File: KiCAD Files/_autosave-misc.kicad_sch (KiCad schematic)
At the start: 16 parts, among them U1 K230_Rewired, U6 GT-USB-7013A03, Y1 32.768KHz, Y2 32.768KHz

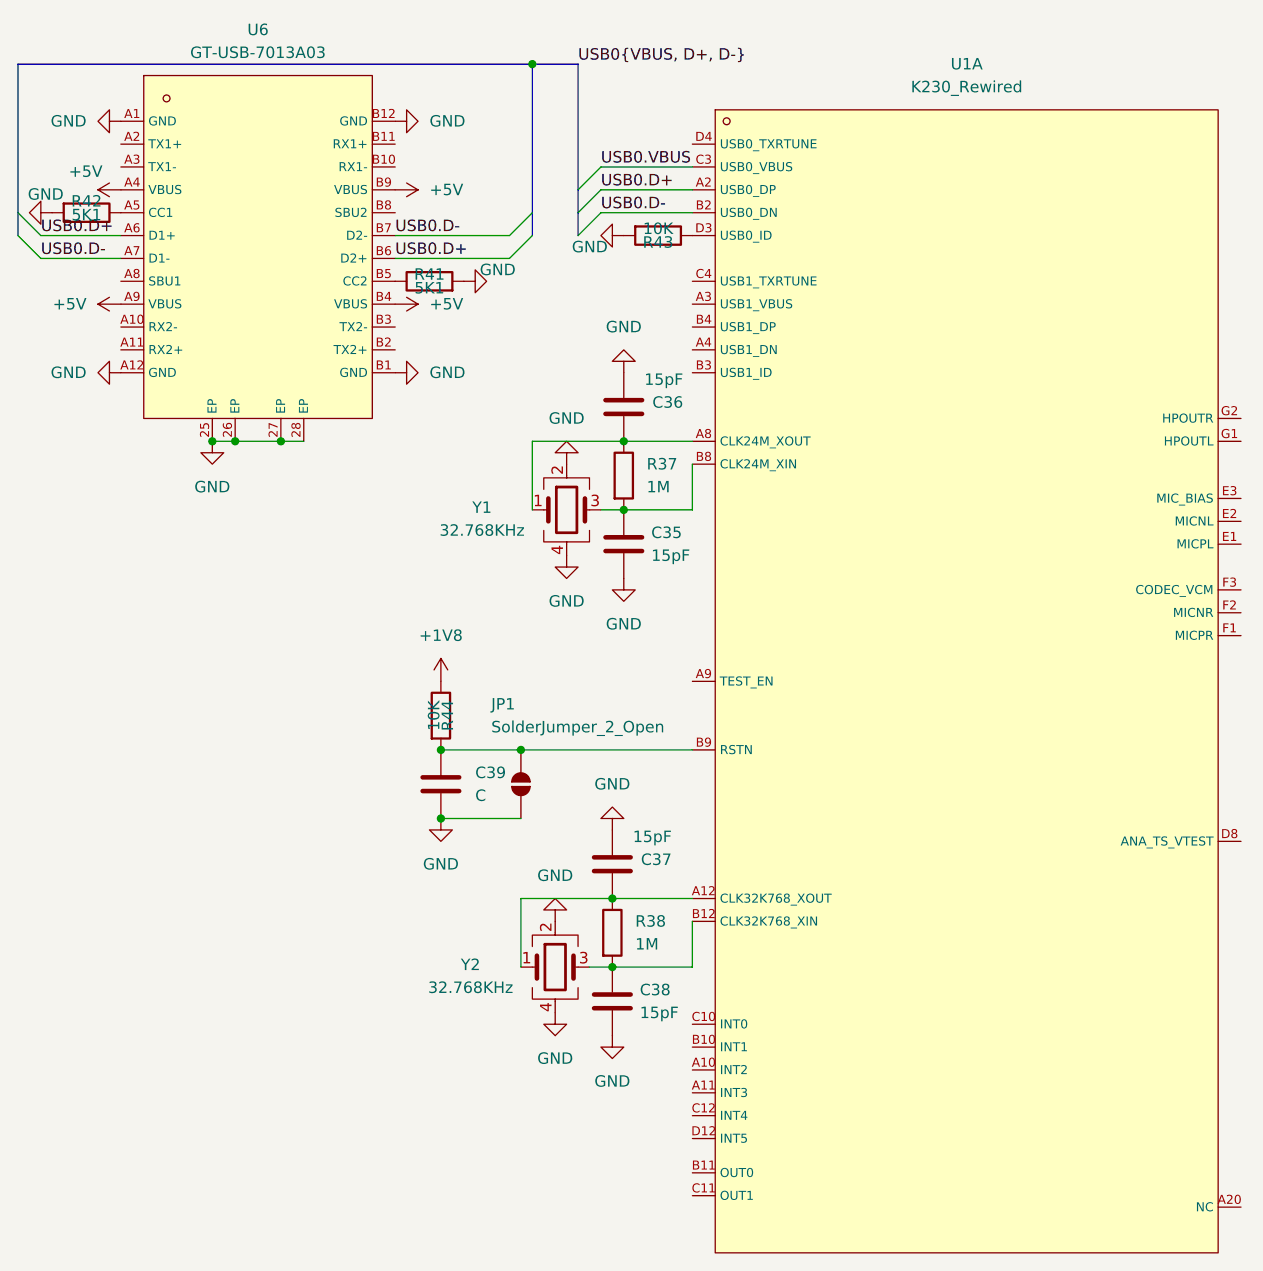
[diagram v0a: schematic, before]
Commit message: more peripherals
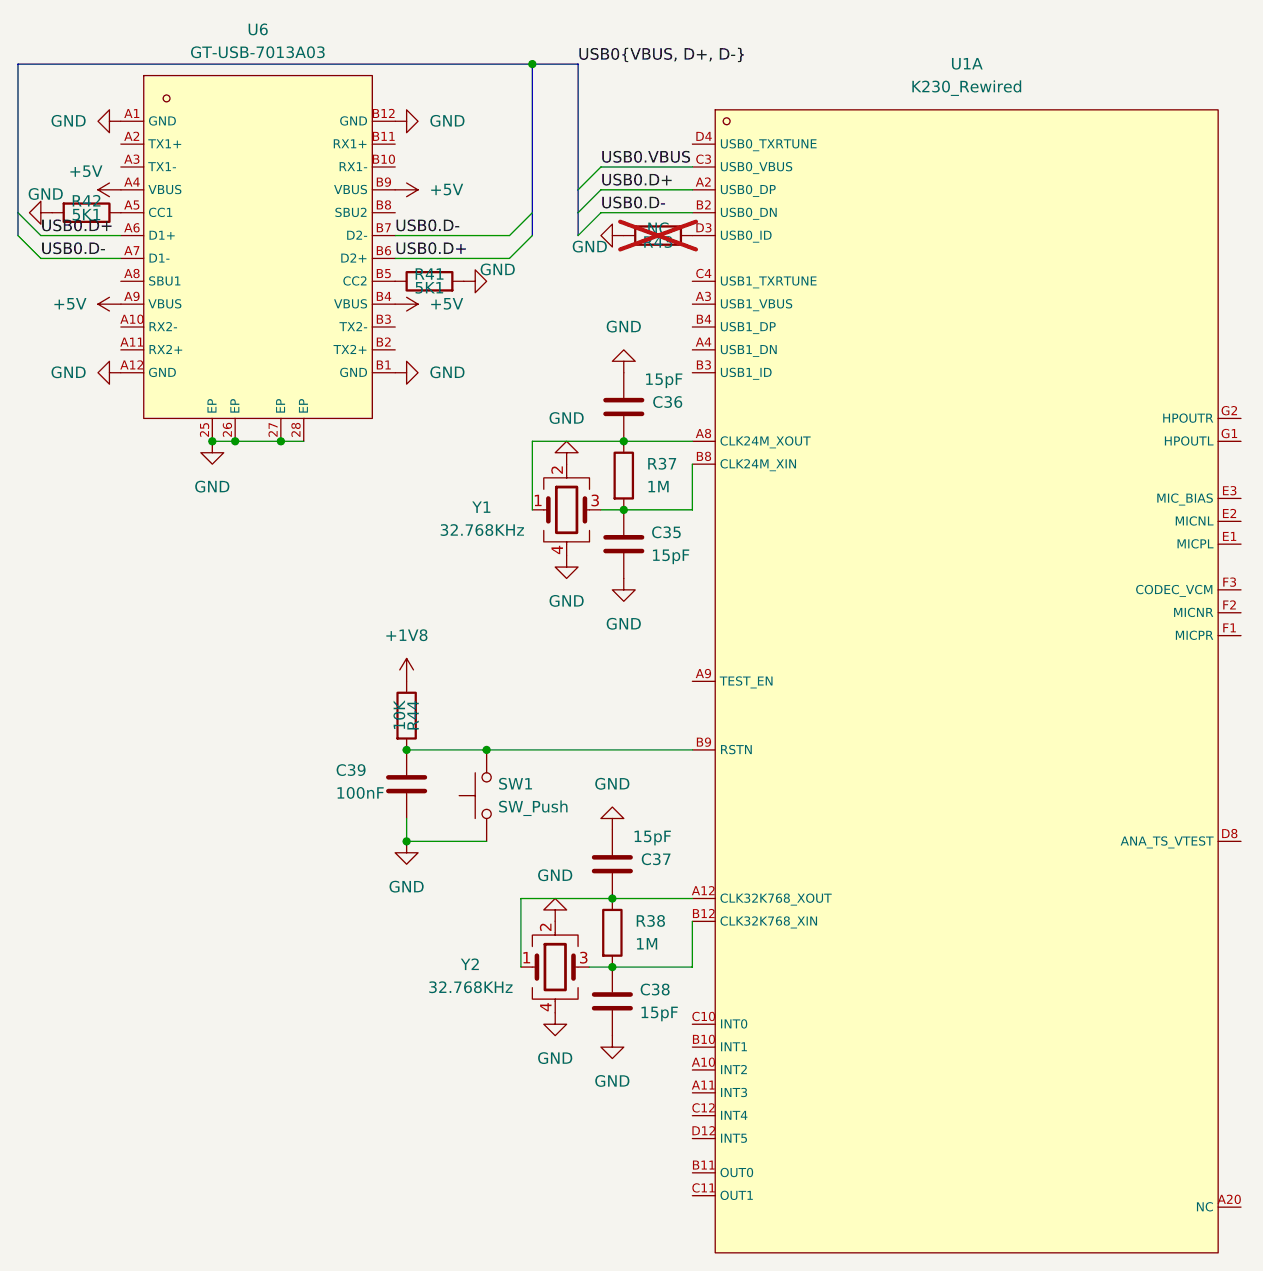
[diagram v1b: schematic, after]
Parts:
- removed JP1: SolderJumper_2_Open, Jumper:SolderJumper-2_P1.3mm_Open_TrianglePad1.0x1.5mm, symbol Jumper:SolderJumper_2_Open
- added SW1: SW_Push, Button_Switch_THT:SW_PUSH_1P1T_6x3.5mm_H4.3_APEM_MJTP1243, symbol Switch:SW_Push
- C39: value C -> 100nF
- R43: value 10K -> NC; now not fitted; now left out of the parts list
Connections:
- net GND: now also SW1.1
- net at C39.1, R44.2, U1.B9 (RSTN): now also SW1.2
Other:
- moved on the sheet: C39, R44
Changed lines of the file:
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@@
 	)
 	(junction
-		(at 110.49 99.06)
-		(diameter 0)
-		(color 0 0 0 0)
-	)
-	(junction
 		(at 76.2 64.77)
 		(diameter 0)
@@
 	)
 	(junction
-		(at 101.6 99.06)
+		(at 97.79 99.06)
+		(diameter 0)
+		(color 0 0 0 0)
+	)
+	(junction
+		(at 97.79 109.22)
 		(diameter 0)
 		(color 0 0 0 0)
@@
 	)
 	(junction
-		(at 101.6 106.68)
+		(at 106.68 99.06)
 		(diameter 0)
 		(color 0 0 0 0)
@@
 	(wire
 		(pts
+			(xy 97.79 109.22) (xy 97.79 106.68)
+		)
+		(stroke
+			(width 0)
+			(type default)
+		)
+	)
+	(wire
+		(pts
 			(xy 83.82 64.77) (xy 86.36 64.77)
 		)
@@
 	(wire
 		(pts
-			(xy 101.6 99.06) (xy 110.49 99.06)
+			(xy 97.79 99.06) (xy 106.68 99.06)
 		)
 		(stroke
@@
 	(wire
 		(pts
-			(xy 110.49 99.06) (xy 129.54 99.06)
+			(xy 106.68 99.06) (xy 129.54 99.06)
 		)
 		(stroke
@@
 	(wire
 		(pts
-			(xy 101.6 106.68) (xy 110.49 106.68)
+			(xy 97.79 109.22) (xy 106.68 109.22)
 		)
 		(stroke
@@
 	(symbol
 		(lib_id "Device:C")
-		(at 101.6 102.87 0)
+		(at 97.79 102.87 0)
 		(unit 1)
 		(exclude_from_sim no)
@@
 		(on_board yes)
 		(dnp no)
-		(fields_autoplaced yes)
 		(property "Reference" "C39"
-			(at 105.41 101.5999 0)
+			(at 89.916 101.346 0)
 			(effects
 				(font
@@
 			)
 		)
-		(property "Value" "C"
-			(at 105.41 104.1399 0)
+		(property "Value" "100nF"
+			(at 89.916 103.886 0)
 			(effects
 				(font
@@
 		)
 		(property "Footprint" "Capacitor_SMD:C_0402_1005Metric"
-			(at 102.5652 106.68 0)
+			(at 98.7552 106.68 0)
 			(effects
 				(font
@@
 		)
 		(property "Datasheet" "~"
-			(at 101.6 102.87 0)
+			(at 97.79 102.87 0)
 			(effects
 				(font
@@
 		)
 		(property "Description" "Unpolarized capacitor"
-			(at 101.6 102.87 0)
+			(at 97.79 102.87 0)
 			(effects
 				(font
@@
 		(at 125.73 41.91 270)
 		(unit 1)
-		(exclude_from_sim no)
-		(in_bom yes)
-		(on_board yes)
-		(dnp no)
+		(exclude_from_sim yes)
+		(in_bom no)
+		(on_board no)
+		(dnp yes)
 		(property "Reference" "R43"
 			(at 125.73 42.672 90)
@@
 			)
 		)
-		(property "Value" "10K"
+		(property "Value" "NC"
 			(at 125.73 41.148 90)
 			(effects
@@
 	(symbol
 		(lib_id "Device:R")
-		(at 101.6 95.25 0)
+		(at 97.79 95.25 0)
 		(unit 1)
 		(exclude_from_sim no)
@@
 		(dnp no)
 		(property "Reference" "R44"
-			(at 102.362 95.25 90)
+			(at 98.552 95.25 90)
 			(effects
 				(font
@@
 		)
 		(property "Value" "10K"
-			(at 100.838 95.25 90)
+			(at 97.028 95.25 90)
 			(effects
 				(font
@@
 		)
 		(property "Footprint" "Resistor_SMD:R_0402_1005Metric"
-			(at 99.822 95.25 90)
+			(at 96.012 95.25 90)
 			(effects
 				(font
@@
 		)
 		(property "Datasheet" "~"
-			(at 101.6 95.25 0)
+			(at 97.79 95.25 0)
 			(effects
 				(font
@@
 		)
 		(property "Description" "Resistor"
-			(at 101.6 95.25 0)
+			(at 97.79 95.25 0)
 			(effects
 				(font
@@
 	)
 	(symbol
+		(lib_id "Switch:SW_Push")
+		(at 106.68 104.14 90)
+		(unit 1)
+		(exclude_from_sim no)
+		(in_bom yes)
+		(on_board yes)
+		(dnp no)
+		(fields_autoplaced yes)
+		(property "Reference" "SW1"
+			(at 107.95 102.8699 90)
+			(effects
+				(font
+					(size 1.27 1.27)
+				)
+				(justify right)
+			)
+		)
+		(property "Value" "SW_Push"
+			(at 107.95 105.4099 90)
+			(effects
+				(font
+					(size 1.27 1.27)
+				)
+				(justify right)
+			)
+		)
+		(property "Footprint" "Button_Switch_THT:SW_PUSH_1P1T_6x3.5mm_H4.3_APEM_MJTP1243"
+			(at 101.6 104.14 0)
+			(effects
+				(font
+					(size 1.27 1.27)
+				)
+				(hide yes)
+			)
+		)
+		(property "Datasheet" "~"
+			(at 101.6 104.14 0)
+			(effects
+				(font
+					(size 1.27 1.27)
+				)
+				(hide yes)
+			)
+		)
+		(property "Description" "Push button switch, generic, two pins"
+			(at 106.68 104.14 0)
+			(effects
+				(font
+					(size 1.27 1.27)
+				)
+				(hide yes)
+			)
+		)
+		(pin "2"
+		)
+		(pin "1"
+		)
+		(instances
+			(project ""
+				(path "/162c5a9c-1e99-4dd0-95df-e63e36263ff0/f7ff160e-8568-4505-a6c1-180ade093d2e"
+					(reference "SW1")
+					(unit 1)
+				)
+			)
+		)
+	)
+	(symbol
 		(lib_id "Device:C")
 		(at 120.65 111.76 180)
@@
 	(symbol
 		(lib_id "power:GND")
-		(at 101.6 106.68 0)
+		(at 97.79 109.22 0)
 		(unit 1)
 		(exclude_from_sim no)
@@
 		(fields_autoplaced yes)
 		(property "Reference" "#PWR060"
-			(at 101.6 113.03 0)
+			(at 97.79 115.57 0)
 			(effects
 				(font
@@
 		)
 		(property "Value" "GND"
-			(at 101.6 111.76 0)
+			(at 97.79 114.3 0)
 			(effects
 				(font
@@
 		)
 		(property "Footprint" ""
-			(at 101.6 106.68 0)
+			(at 97.79 109.22 0)
 			(effects
 				(font
@@
 		)
 		(property "Datasheet" ""
-			(at 101.6 106.68 0)
+			(at 97.79 109.22 0)
 			(effects
 				(font
@@
 		)
 		(property "Description" "Power symbol creates a global label with name \"GND\" , ground"
-			(at 101.6 106.68 0)
+			(at 97.79 109.22 0)
 			(effects
 				(font
@@
 	(symbol
 		(lib_id "power:+1V8")
-		(at 101.6 91.44 0)
+		(at 97.79 91.44 0)
 		(unit 1)
 		(exclude_from_sim no)
@@
 		(fields_autoplaced yes)
 		(property "Reference" "#PWR059"
-			(at 101.6 95.25 0)
+			(at 97.79 95.25 0)
 			(effects
 				(font
@@
 		)
 		(property "Value" "+1V8"
-			(at 101.6 86.36 0)
+			(at 97.79 86.36 0)
 			(effects
 				(font
@@
 		)
 		(property "Footprint" ""
-			(at 101.6 91.44 0)
+			(at 97.79 91.44 0)
 			(effects
 				(font
@@
 		)
 		(property "Datasheet" ""
-			(at 101.6 91.44 0)
+			(at 97.79 91.44 0)
 			(effects
 				(font
@@
 		)
 		(property "Description" "Power symbol creates a global label with name \"+1V8\""
-			(at 101.6 91.44 0)
+			(at 97.79 91.44 0)
 			(effects
 				(font
@@
 					(unit 1)
 				)
-			)
-		)
-	)
-	(symbol
-		(lib_id "Jumper:SolderJumper_2_Open")
-		(at 110.49 102.87 90)
-		(unit 1)
-		(exclude_from_sim no)
-		(in_bom no)
-		(on_board yes)
-		(dnp no)
-		(property "Reference" "JP1"
-			(at 107.188 93.98 90)
-			(effects
-				(font
-					(size 1.27 1.27)
-				)
-				(justify right)
-			)
-		)
-		(property "Value" "SolderJumper_2_Open"
-			(at 107.188 96.52 90)
-			(effects
-				(font
-					(size 1.27 1.27)
-				)
-				(justify right)
-			)
-		)
-		(property "Footprint" "Jumper:SolderJumper-2_P1.3mm_Open_TrianglePad1.0x1.5mm"
-			(at 110.49 102.87 0)
-			(effects
-				(font
-					(size 1.27 1.27)
-				)
-				(hide yes)
-			)
-		)
-		(property "Datasheet" "~"
-			(at 110.49 102.87 0)
-			(effects
-				(font
-					(size 1.27 1.27)
-				)
-				(hide yes)
-			)
-		)
-		(property "Description" "Solder Jumper, 2-pole, open"
-			(at 110.49 102.87 0)
-			(effects
-				(font
-					(size 1.27 1.27)
-				)
-				(hide yes)
-			)
-		)
-		(pin "2"
-		)
-		(pin "1"
-		)
-		(instances
-			(project ""
-				(path "/162c5a9c-1e99-4dd0-95df-e63e36263ff0/f7ff160e-8568-4505-a6c1-180ade093d2e"
-					(reference "JP1")
-					(unit 1)
-				)
